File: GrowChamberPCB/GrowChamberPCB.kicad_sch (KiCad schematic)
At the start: 5 parts, among them J1 Screw_Terminal_01x02

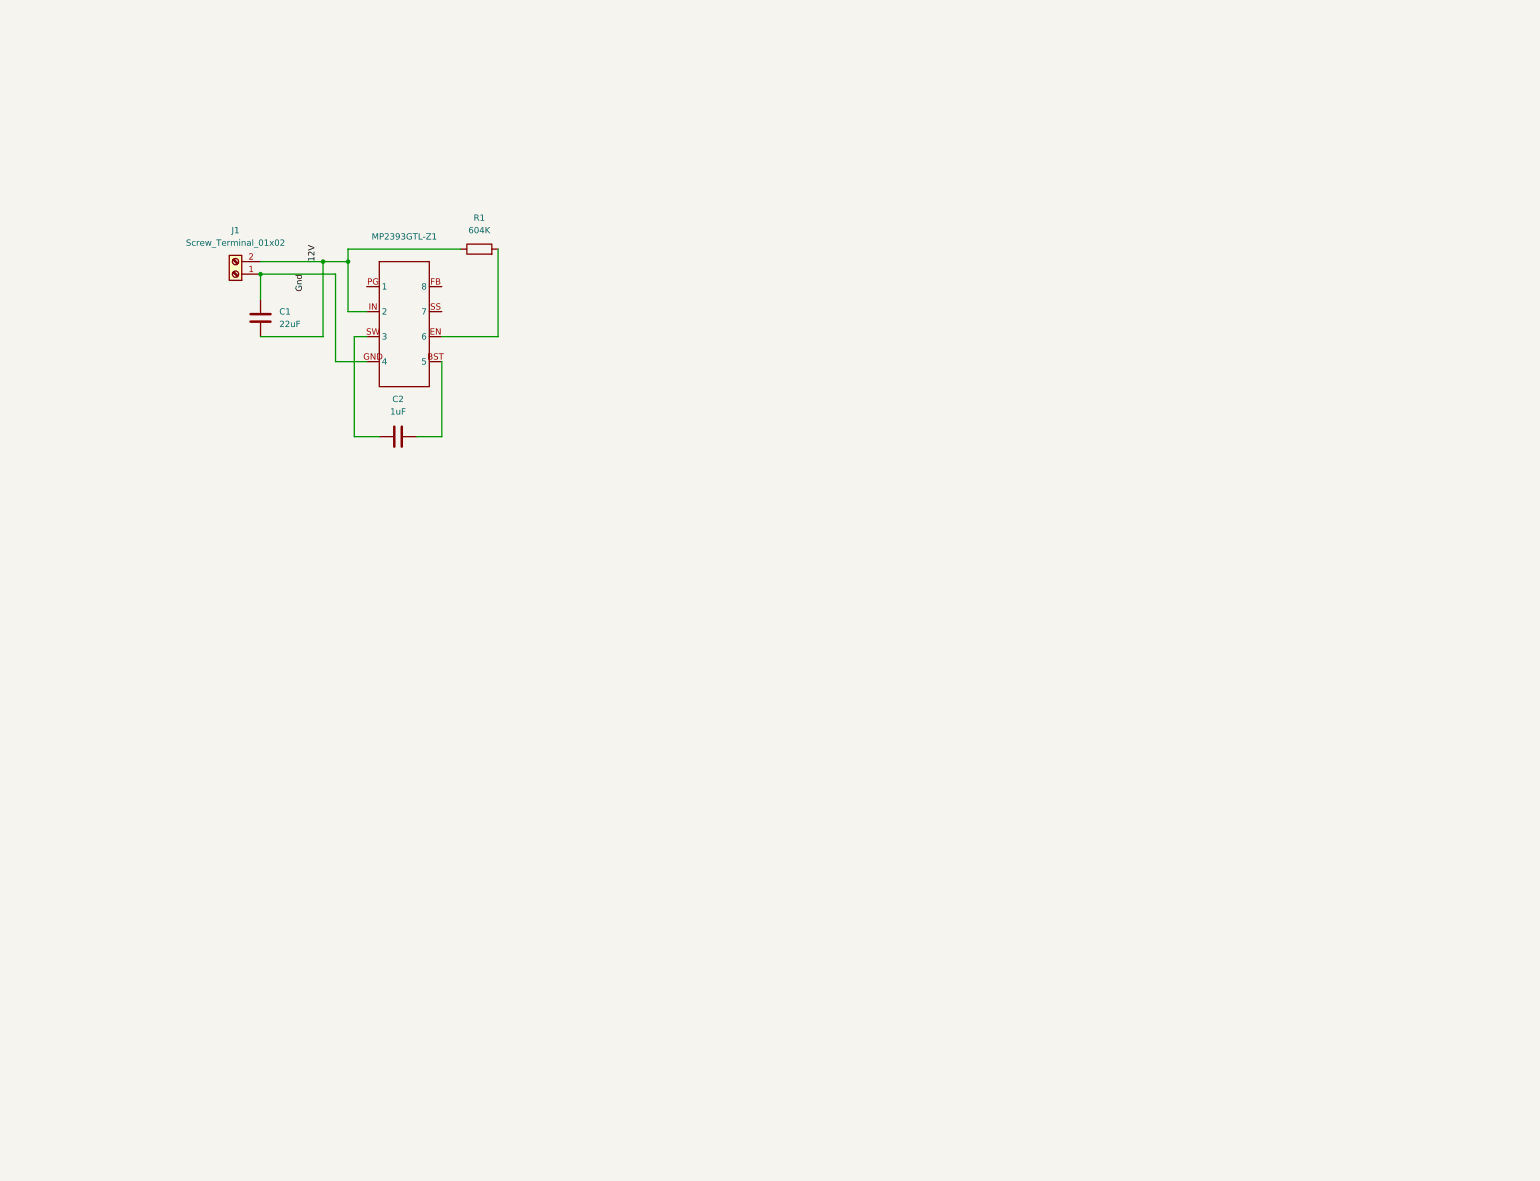
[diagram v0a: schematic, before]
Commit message: Power added to board
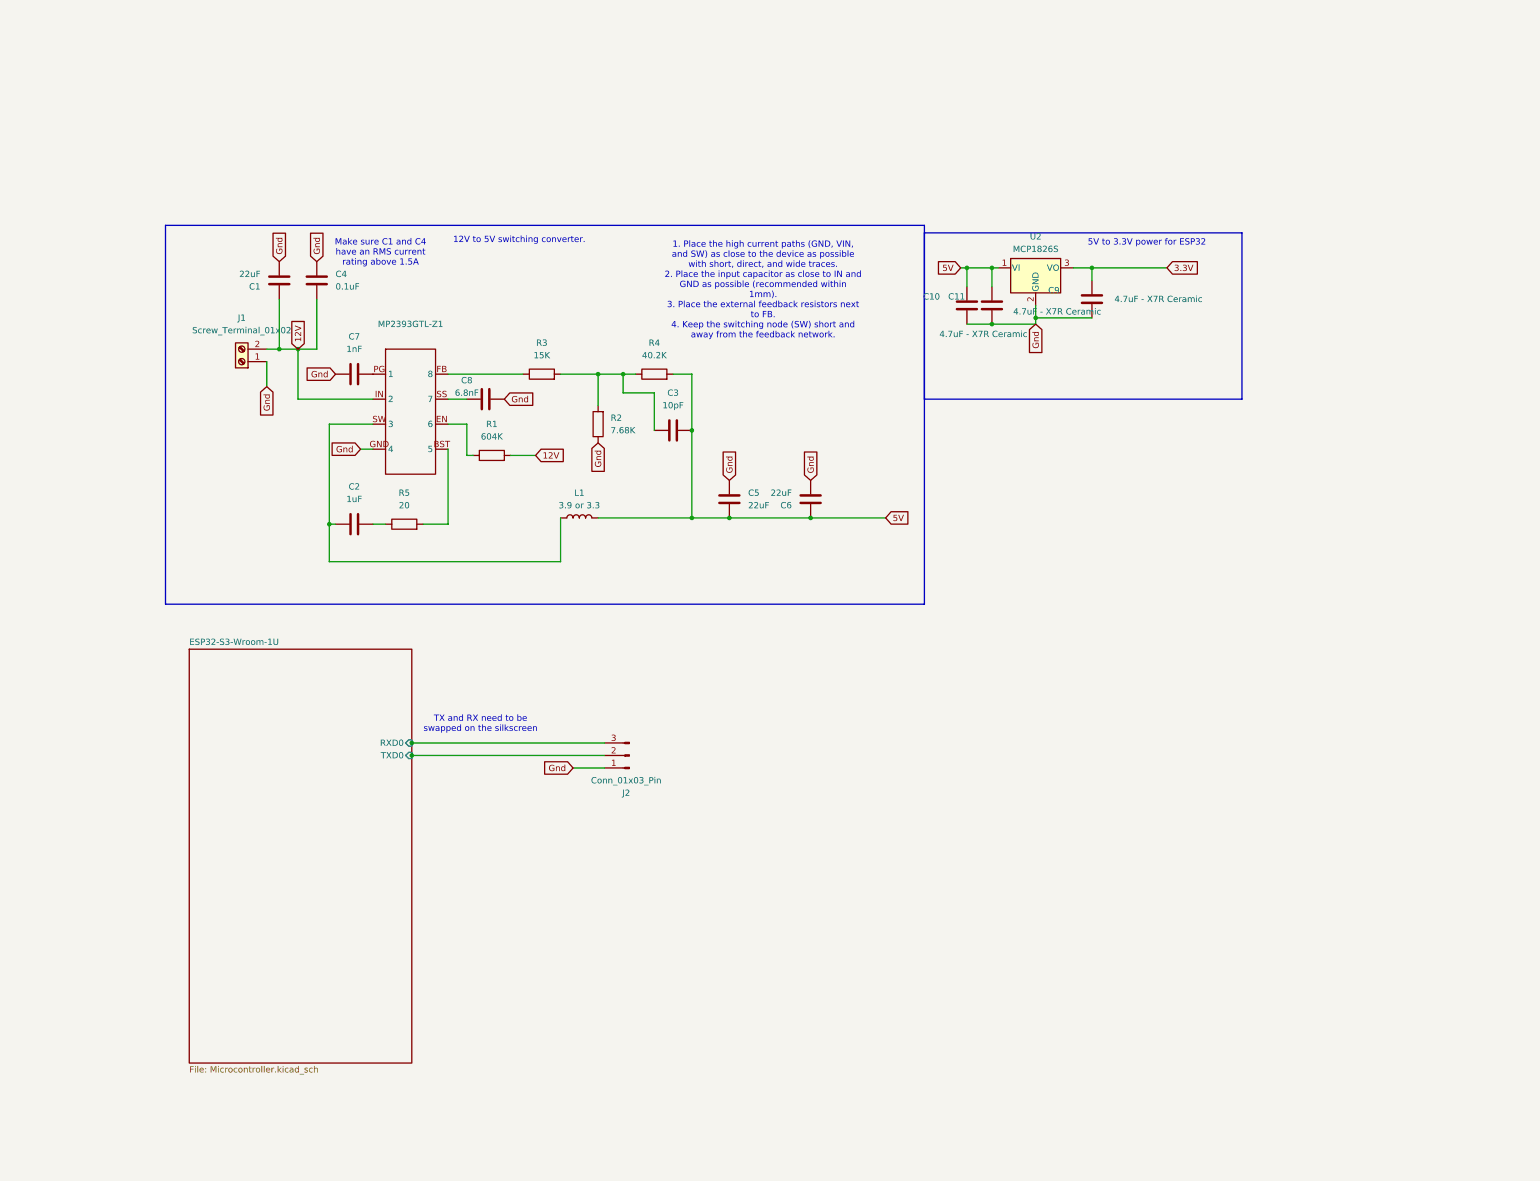
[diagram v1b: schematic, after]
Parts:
- added C10, C11, C9: 4.7uF - X7R Ceramic, symbol Device:C
- added C3: 10pF, symbol Device:C
- added C4: 0.1uF, symbol Device:C
- added C5, C6: 22uF, symbol Device:C
- added C7: 1nF, symbol Device:C
- added C8: 6.8nF, symbol Device:C
- added J2: Conn_01x03_Pin, symbol Connector:Conn_01x03_Pin
- added L1: 3.9 or 3.3, symbol Device:L
- added R2: 7.68K, symbol Device:R
- added R3: 15K, symbol Device:R
- added R4: 40.2K, symbol Device:R
- added R5: 20, symbol Device:R
- added U2: MCP1826S, Package_TO_SOT_SMD:SOT-223-3_TabPin2, symbol Regulator_Linear:MCP1826S
- MP2393GTL-Z1: footprint (none) -> Package_TO_SOT_SMD:SOT-583-8
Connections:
- net 12V: now also C1.1, R1.2, C4.1; no longer C1.2, R1.1
- net Gnd: now also C1.2, C10.2, C11.2, C4.2, C5.2, C6.2, C7.2, C8.1, C9.2, J2.1 (Pin_1), R2.1, U2.2 (GND); no longer C1.1
- net at C2.2: now also R5.1; no longer MP2393GTL-Z1.BST (5)
- net at MP2393GTL-Z1.EN (6): now also R1.1; no longer R1.2
- net at MP2393GTL-Z1.FB (8): now also R3.1
- net at MP2393GTL-Z1.PG (1): now also C7.1
- net at MP2393GTL-Z1.SS (7): now also C8.2
- net at C2.1, MP2393GTL-Z1.SW (3): now also L1.1
- new net: C3.2, R2.2, R3.2, R4.1
- new net: MP2393GTL-Z1.BST (5), R5.2
- new net 3.3V: C9.1, U2.3 (VO)
- new net 5V: C10.1, C11.1, C3.1, C5.1, C6.1, L1.2, R4.2, U2.1 (VI)
- new net ESP32-S3-Wroom-1U/RXD0: J2.3 (Pin_3)
- new net ESP32-S3-Wroom-1U/TXD0: J2.2 (Pin_2)
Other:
- added sheet ESP32-S3-Wroom-1U (Microcontroller.kicad_sch)
- note added: "1. Place the high current paths (GND, VIN, and SW) as close to the device as possible with short, direct, and wide traces. 2. Place the input capacitor as close to IN and GND as possible (recommended within 1mm). 3. Place the external feedback resistors next to FB. 4. Keep the switching node (SW) short and away from the feedback network."
- note added: "12V to 5V switching converter."
- note added: "5V to 3.3V power for ESP32"
- note added: "Make sure C1 and C4 have an RMS current rating above 1.5A"
- note added: "TX and RX need to be swapped on the silkscreen"
- moved on the sheet: C1, C2, J1, MP2393GTL-Z1, R1

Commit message: some USB stuff
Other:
- sheet ESP32-S3-Wroom-1U ports: added D+, D-, VBUS; removed none

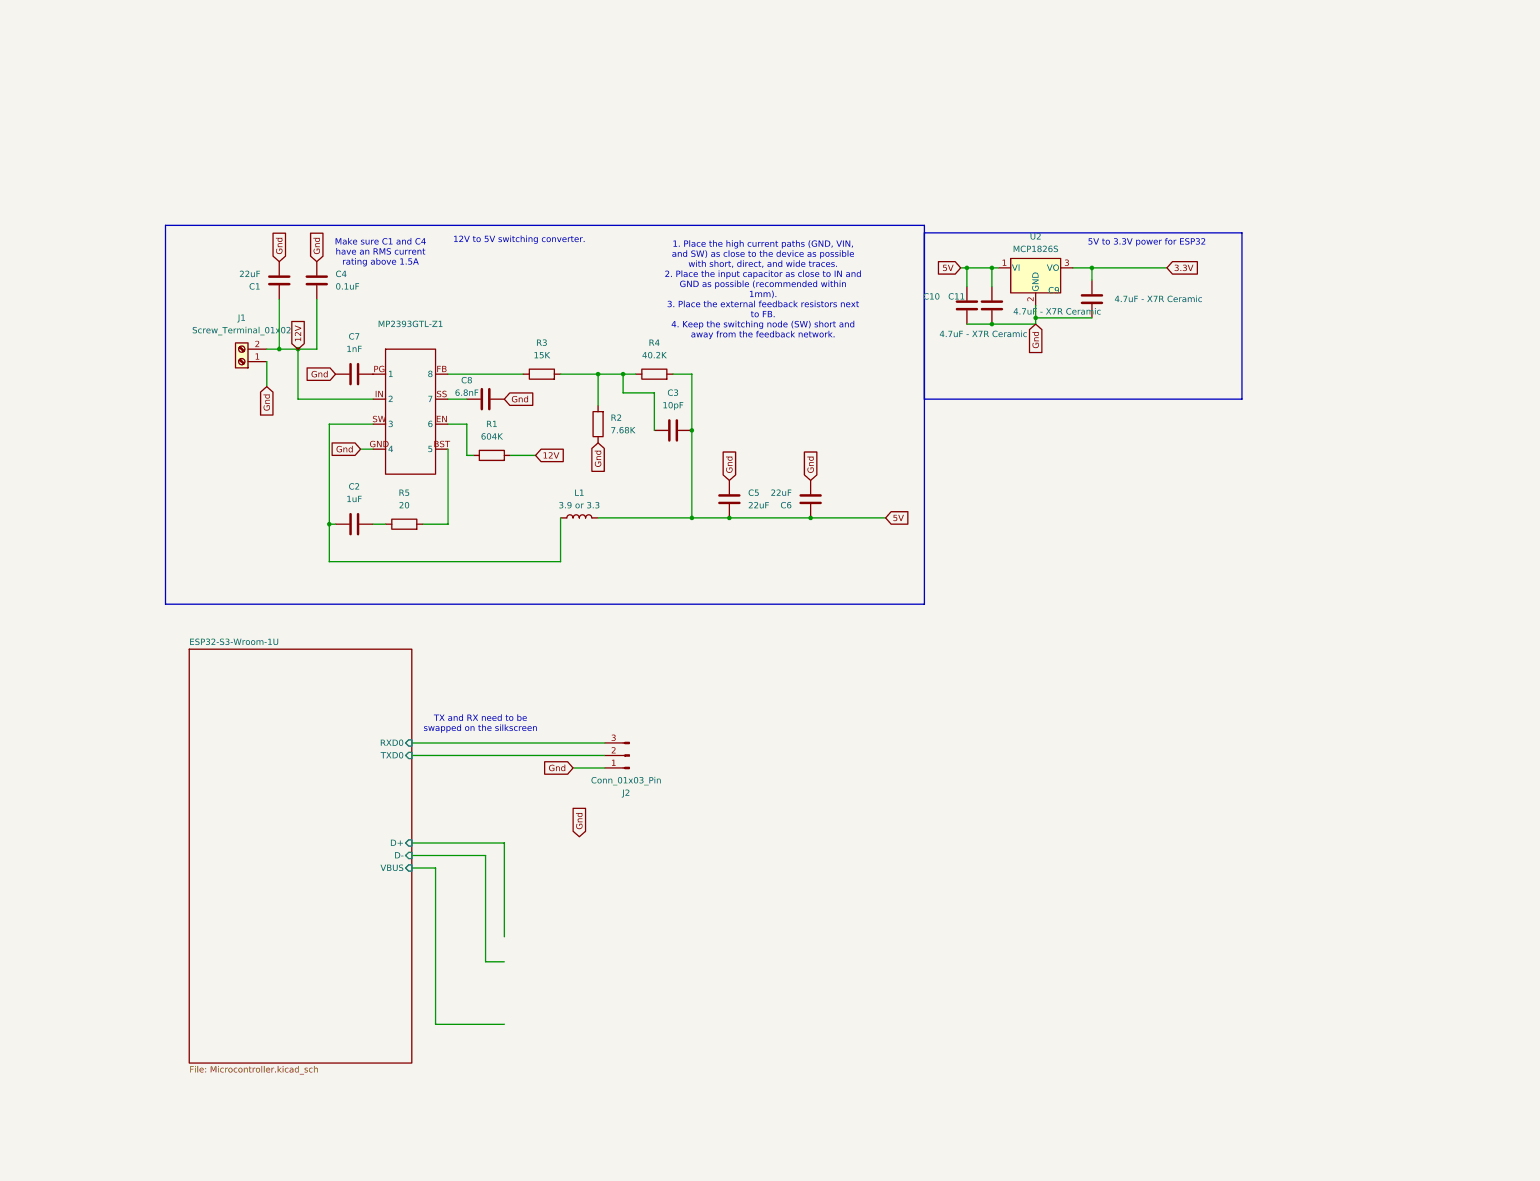
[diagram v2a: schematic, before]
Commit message: USB and buttons added to schematic
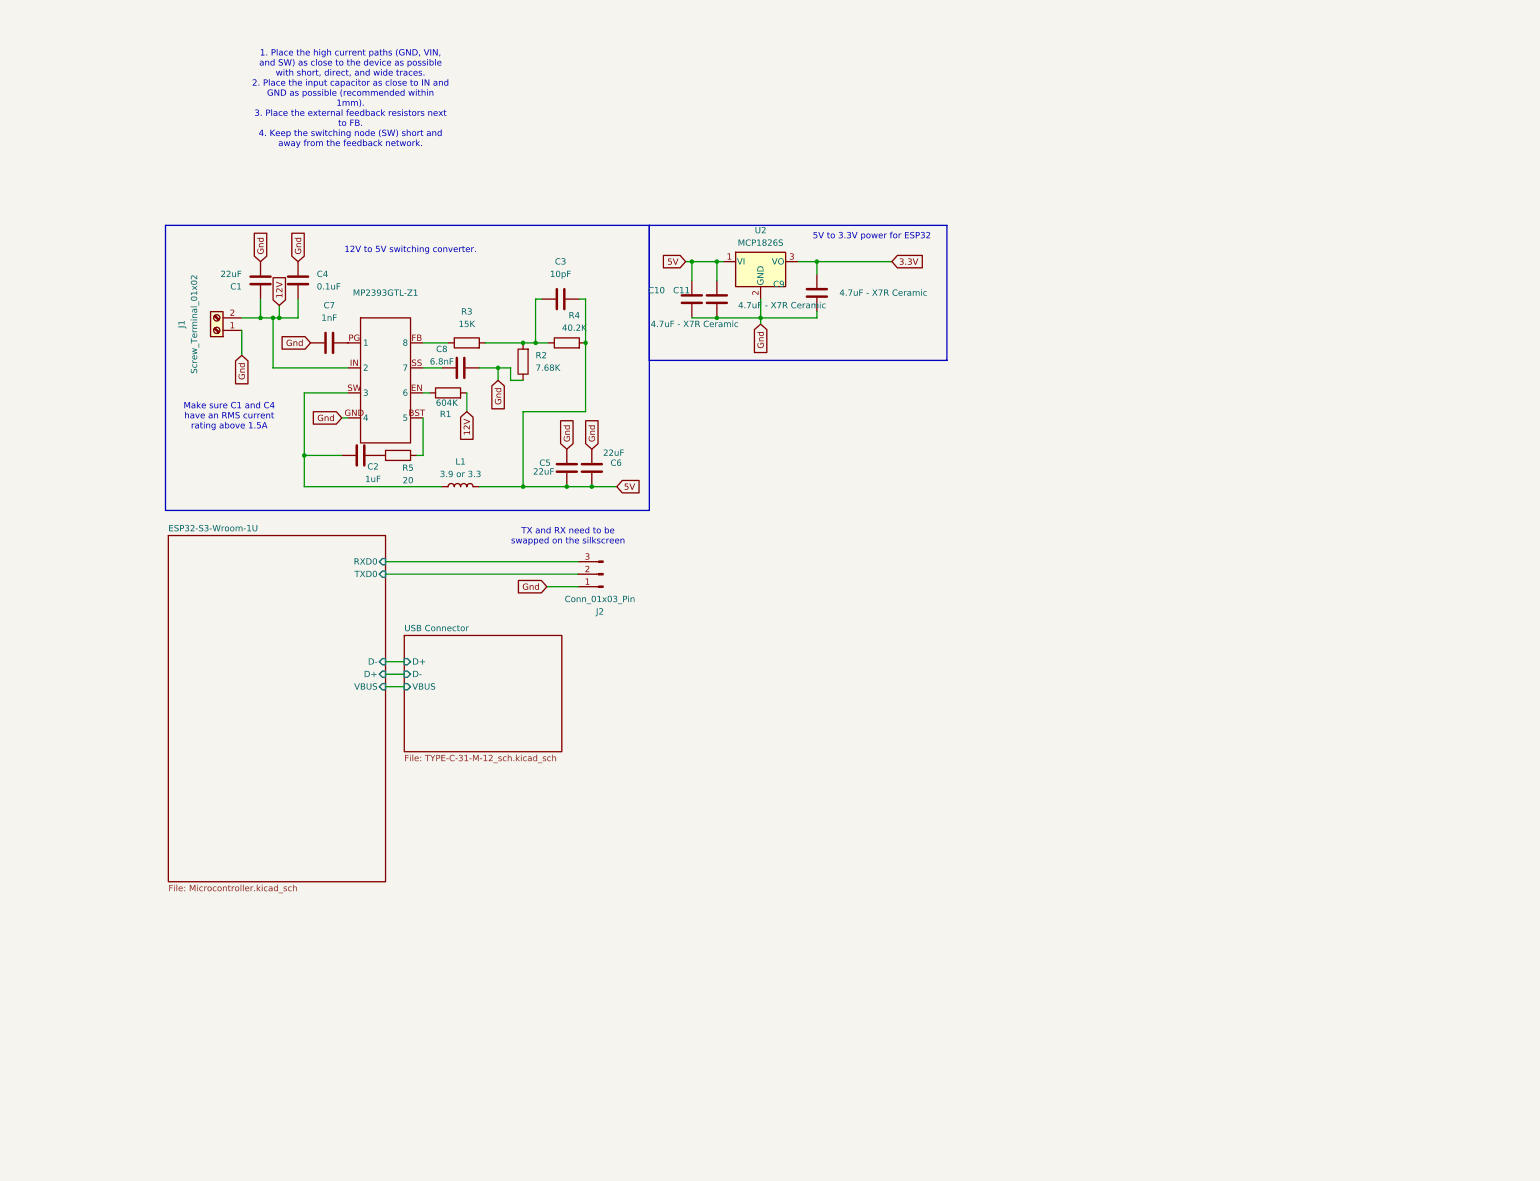
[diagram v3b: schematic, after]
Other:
- added sheet USB Connector (TYPE-C-31-M-12_sch.kicad_sch)
- moved on the sheet: C1, C10, C11, C2, C3, C4, C5, C6, C7, C8, C9, J1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

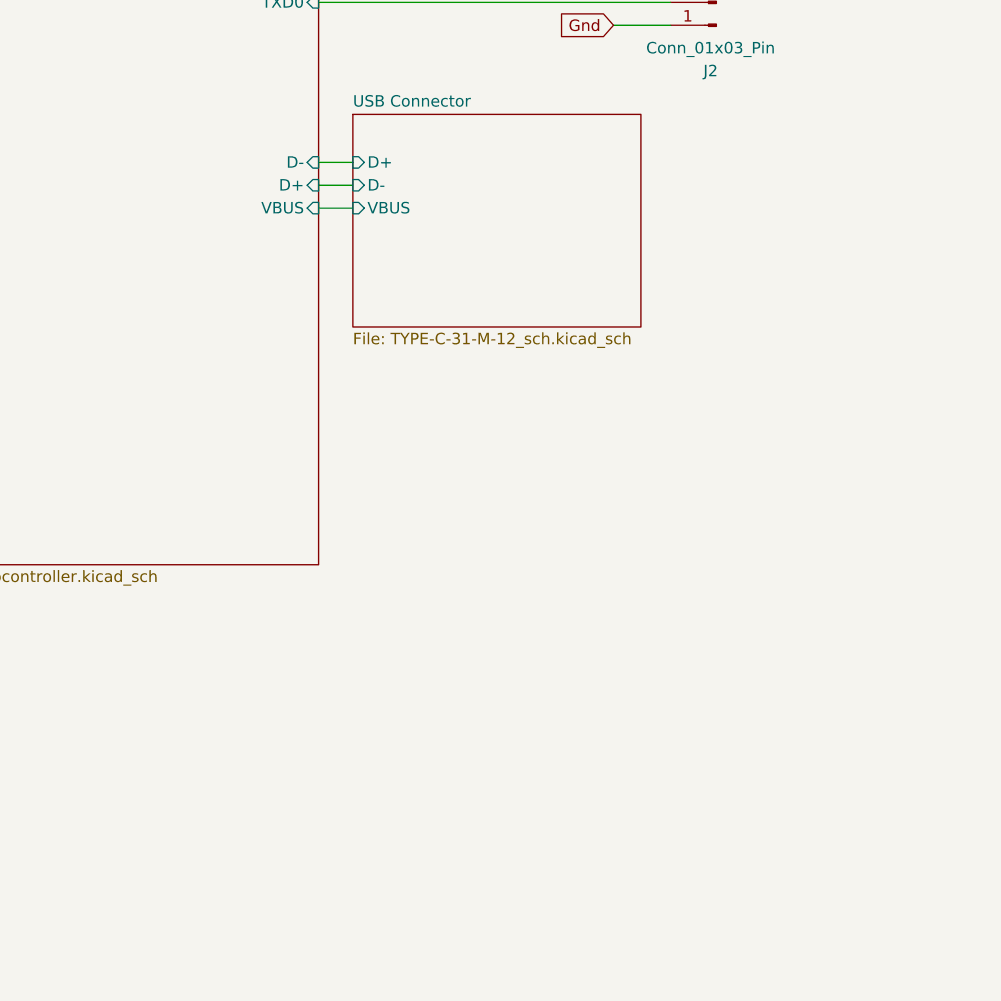
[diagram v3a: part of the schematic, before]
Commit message: GPIO labeling and mist maker added
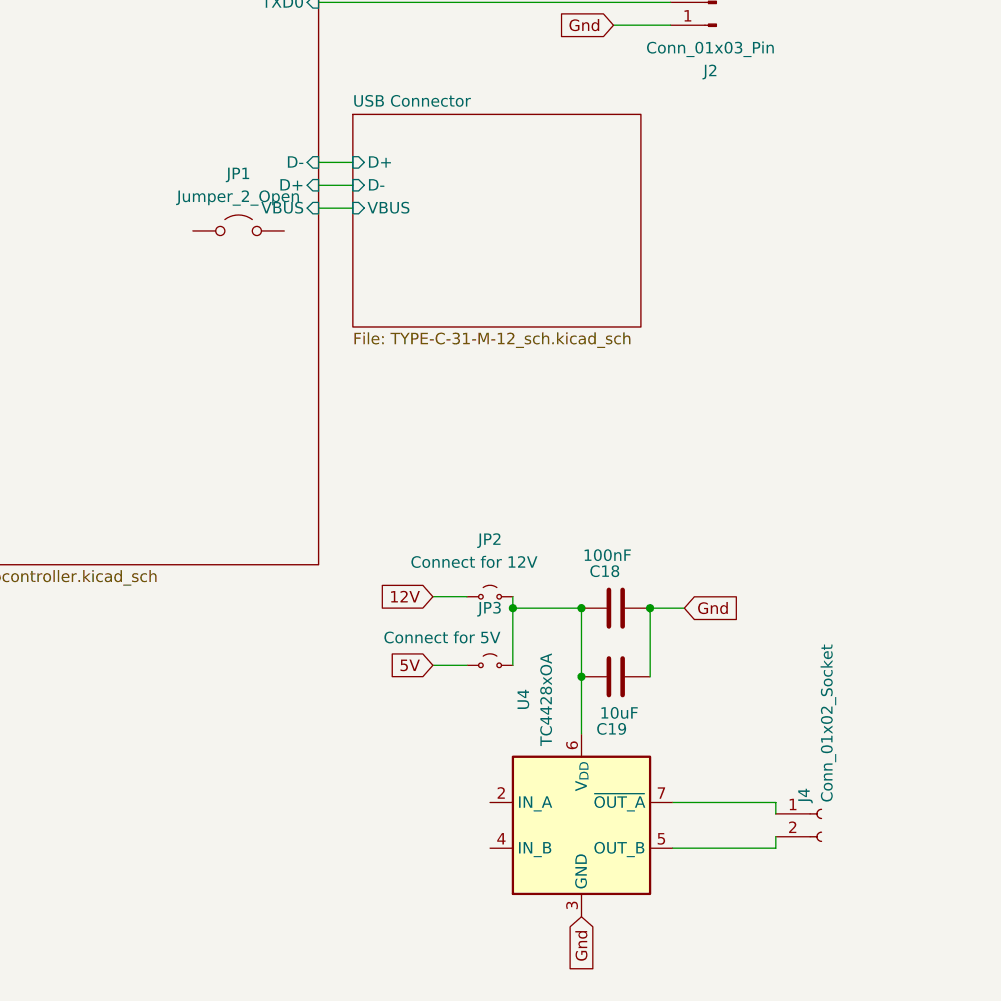
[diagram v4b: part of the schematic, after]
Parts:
- added C18: 100nF, symbol Device:C
- added C19: 10uF, symbol Device:C
- added J4: Conn_01x02_Socket, symbol Connector:Conn_01x02_Socket
- added JP1: Jumper_2_Open, symbol Jumper:Jumper_2_Open
- added JP2: Connect for 12V, symbol Jumper:Jumper_2_Small_Open
- added JP3: Connect for 5V, symbol Jumper:Jumper_2_Small_Open
- added U4: TC4428xOA, Package_SO:SOIC-8_3.9x4.9mm_P1.27mm, symbol Driver_FET:TC4428xOA
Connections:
- net 12V: now also JP2.1 (A)
- net 5V: now also JP3.1 (A)
- net Gnd: now also C18.1, C19.1, U4.3 (GND)
- new net: J4.2 (Pin_2), U4.5 (OUT_B)
- new net: C18.2, C19.2, JP2.2 (B), JP3.2 (B), U4.6 (V_{DD})
- new net: J4.1 (Pin_1), U4.7 (~{OUT_A})

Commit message: stuff
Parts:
- removed JP1: Jumper_2_Open, symbol Jumper:Jumper_2_Open
- added U5: W25Q128JVS, Package_SO:SOIC-8_5.3x5.3mm_P1.27mm, symbol Memory_Flash:W25Q128JVS
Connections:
- net Gnd: now also U5.4 (GND)
- new net CS_Memory / GPIO4: U5.1 (~{CS})
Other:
- moved on the sheet: C18, C19, J4, JP2, JP3, U4
